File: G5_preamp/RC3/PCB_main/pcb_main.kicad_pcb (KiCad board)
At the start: 2 copper layers, 165 x 58 mm, 57 parts, among them J1 PSU_TUBE, J2 PCB_TUBE, J3 PSU_AMP, J4 AMP, J5 PSU_SIMCAB, J6 SIMCAB, J7 3PDT, J8 LEVEL 3-2, Q1 MPS751, Q2 IRF740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

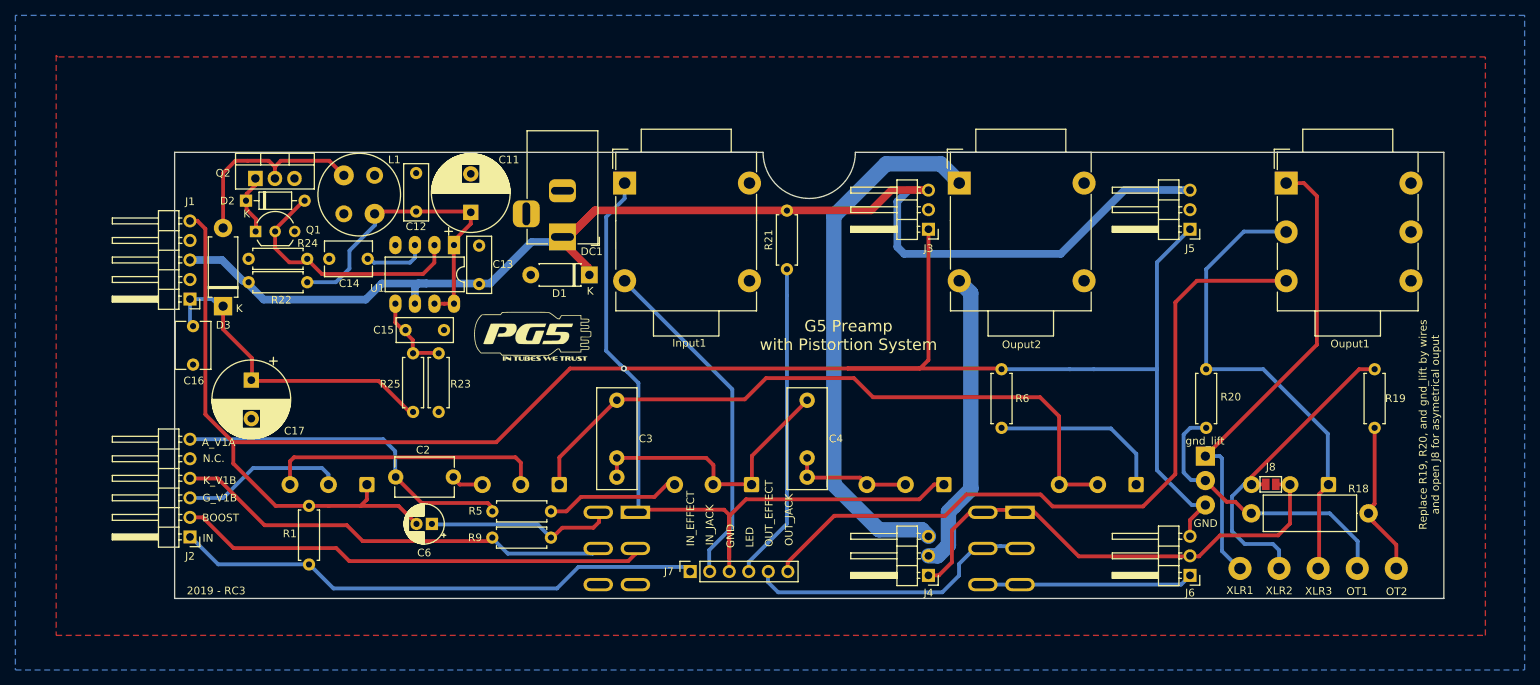
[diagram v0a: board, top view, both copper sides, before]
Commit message: RC3 update
Cathode Cap change 3d models and place (pcb-main)
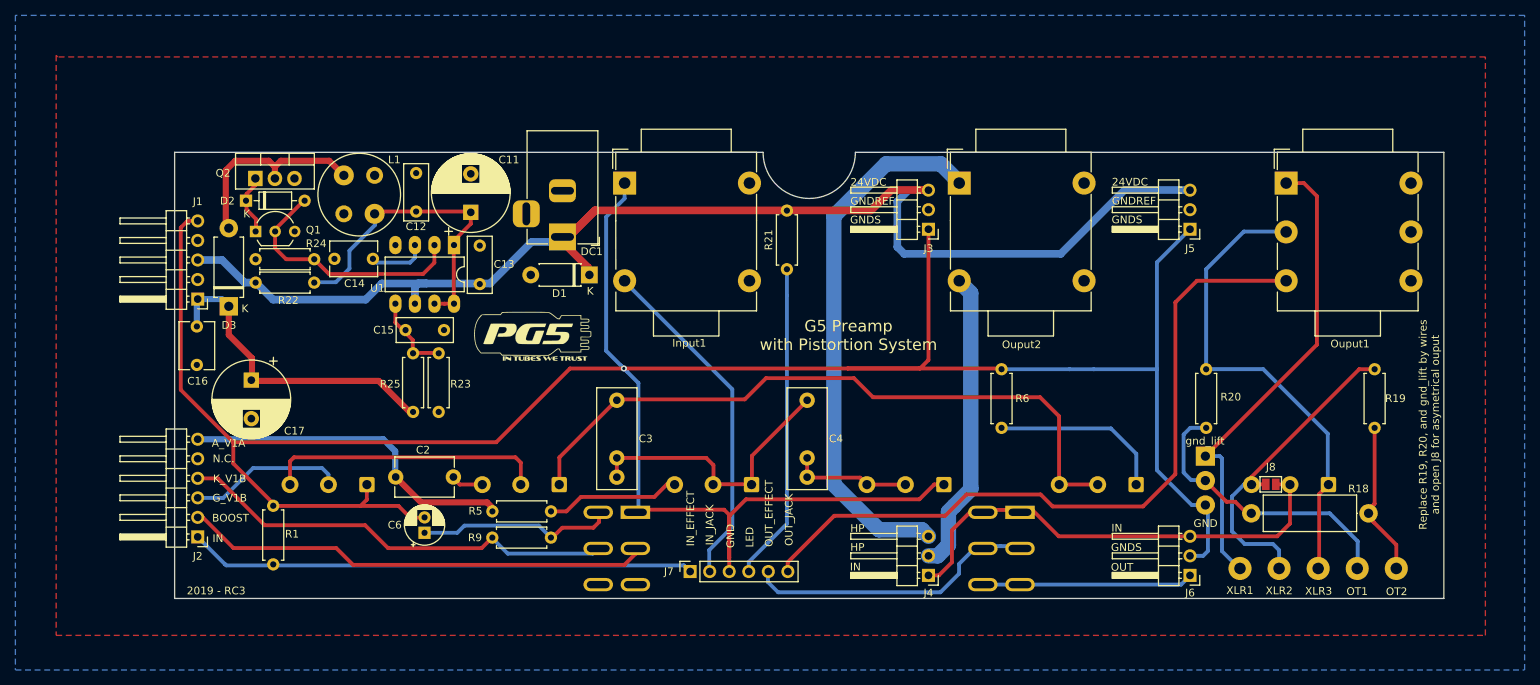
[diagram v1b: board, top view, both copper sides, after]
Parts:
- moved R1 4.65 mm to (92.8, 155.6)
- moved C6 1.49 mm to (112.5, 151.5), turned to 90 degrees
- moved J1 1.00 mm to (83.0, 121.1)
- moved J2 1.00 mm to (83.0, 152.0)
- moved R24 0.91 mm to (98.2, 115.9)
- moved R22 0.91 mm to (90.5, 118.9)
- moved D3 0.74 mm to (87.0, 122.0)
- moved C14 0.68 mm to (105.8, 115.8)
- moved C16 0.49 mm to (82.9, 124.6)
- moved C13 0.08 mm to (119.7, 119.1)
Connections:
- C3 pad 3: Net-(C3-Pad2) -> (no net)
- C4 pad 3: Net-(C4-Pad2) -> (no net)
- J6 pad 2: /LINE_OUT -> GNDS
- J6 pad 3: GNDS -> /LINE_OUT
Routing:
- net GNDS: track 363.9 -> 370.0 mm
- net /IN_EFFECT: track 69.1 -> 65.9 mm
- net /LINE_OUT: track 63.9 -> 61.7 mm
- net +24V: track 172.5 -> 171.1 mm
- net /G_V1B: track 21.6 -> 20.2 mm
- net Net-(C6-Pad1): track 24.5 -> 25.8 mm
- net /A_V1A: track 44.8 -> 43.8 mm
- net /PEAK: track 42.2 -> 41.4 mm
- net /HT1: track 25.6 -> 26.5 mm
- net Net-(C14-Pad1): track 8.41 -> 7.60 mm
- net /HT2: track 42.3 -> 41.6 mm
- net /BOOST: track 61.6 -> 61.1 mm
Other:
- board text added: "24VDC"
- board text added: "GNDREF"
- board text added: "GNDS"
- board text added: "HP"
- board text added: "HP~"
- board text added: "OUT"

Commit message: RC3 multivoltage
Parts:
- removed GND1: GND, Connector_Wire:SolderWirePad_1x03_P3.175mm_Drill1mm
- removed J8: LEVEL 3-2, Jumper:SolderJumper-2_P1.3mm_Open_Pad1.0x1.5mm
- removed Ouput1: Out, Connector_Audio:Jack_3.5mm_Neutrik_NMJ6HCD2_Horizontal
- removed R20: 330R, Resistor_THT:R_Axial_DIN0207_L6.3mm_D2.5mm_P7.62mm_Horizontal
- removed REF**: PG5_Logo_15mm_SilkScreen, Symbol:PG5_Logo_15mm_SilkScreen
- removed XLR3: 3, Connector_Wire:SolderWirePad_1x01_Drill2mm
- added Output1: Output, ProjectLib_main:Jack_6.35mm_Neutrik_NMJ4HCD2_Horizontal, F.Cu at (224.5, 118.7)
- J2: footprint Connector_PinHeader_2.54mm:PinHeader_1x06_P2.54mm_Horizontal -> Connector_PinHeader_2.54mm:PinHeader_1x07_P2.54mm_Horizontal
- R19: value 330R -> 82k
- moved R19 118.1 mm to (121.3, 158.2), turned to 0 degrees
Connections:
- J1 pad 2: Net-(J1-Pad2) -> (no net)
- J2 pad 5: Net-(J2-Pad5) -> /NFB
- J2 pad 6: /A_V1A -> (no net)
- OT1 pad 1: Net-(GND1-Pad2) -> GNDS
- R18 pad 2: Net-(GND1-Pad2) -> GNDS
- R19 pad 1: Net-(J8-Pad1) -> /NFB
- SW1 pad 3: Net-(SW1-Pad3) -> (no net)
- SW1 pad 6: Net-(SW1-Pad6) -> (no net)
- Volume1 pad 1: Net-(Ouput1-PadR) -> GNDS
- Volume1 pad 3: Net-(J8-Pad1) -> Net-(OT2-Pad1)
- XLR1 pad 1: Net-(GND1-Pad1) -> GNDS
- XLR2 pad 1: Net-(J8-Pad1) -> /OUT_JACK
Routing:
- net Net-(OT2-Pad1): track 20.4 -> 148.5 mm
- net Net-(Ouput1-PadR): track 62.7 -> 0.00 mm
- net Net-(GND1-Pad1): track 62.1 -> 0.00 mm
- net GNDS: track 370.0 -> 428.6 mm
- net /NFB: track 0.00 -> 56.2 mm
- net Net-(J8-Pad1): track 42.1 -> 0.00 mm
- net Net-(GND1-Pad2): track 37.5 -> 0.00 mm
- net /OUT_JACK: track 95.5 -> 131.2 mm
- net /BOOST: track 61.1 -> 63.7 mm
- net /LINE_OUT: track 61.7 -> 59.8 mm
- net /A_V1A: track 43.8 -> 44.9 mm
- net Net-(C6-Pad1): track 25.8 -> 25.0 mm
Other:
- board text added: "+VDC"
- board text added: "NFB"
- board text removed: "24VDC"
- board text removed: "Replace R19, R20, and gnd_lift by wires and open J8 for asymetrical ouput"
- board text removed: "gnd_lift"
